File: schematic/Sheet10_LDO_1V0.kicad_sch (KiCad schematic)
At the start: 6 parts

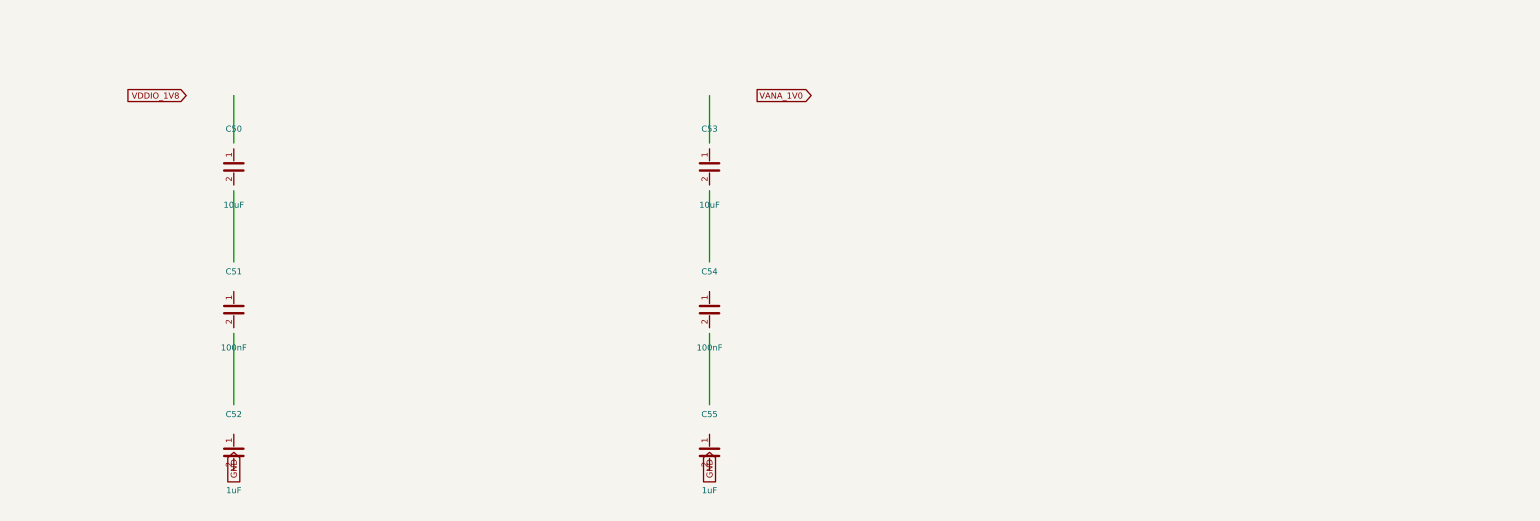
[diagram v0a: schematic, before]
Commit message: feat: real IC schematics with proper pin connections
- ADC12DJ5200-SP: 20 left pins (power, SPI, analog) + 21 right pins (JESD204C)
- XQRVC1902-SP: 19 left pins (power) + 30 right pins (JTAG, SPW, JESD, config)
- TPS7H5002-SP: 9 left + 7 right pins (buck converter 1.0V core)
- ISL70003ASEH: 7 left + 5 right (buck 1.8V/3.3V)
- LMX2615-SP: 8+8 pins (PLL synthesizer)
- LMK04832-SP: 12+12 pins (clock distributor)
- TPS7H1111-SP / TPS7H1121-SP: 3+3 pins (LDOs)
- TPS7H3014-SP: 4+4 pins (sequencer)
- INA214-SP: 3+2 pins (current sense)
- CVHD-950: 3+2 pins (VCXO)

Sheets:
- 02: SMA→50Ω match→anti-alias→ADC analog input
- 03: ADC decoupling, JESD outputs, SPI control
- 04: FPGA 14x decoupling caps, JTAG, SPW, JESD
- 05: Crystek→LMX2615→LMK04832→ADC+FPGA clock tree
- 06-09: Power input, TPS7H5002 buck 1.0V, ISL70003A buck 1.8V/3.3V
- 10-12: LDO 1.0V analog, 1.8V digital, 2.5V clock
- 13: 2x TPS7H3014 power sequencer
- 14: JTAG/SPW/UART connectors
- 15-17: Test points, decoupling, power tree diagram

All 17 sheets export via kicad-cli, merged PDF: 1.1MB
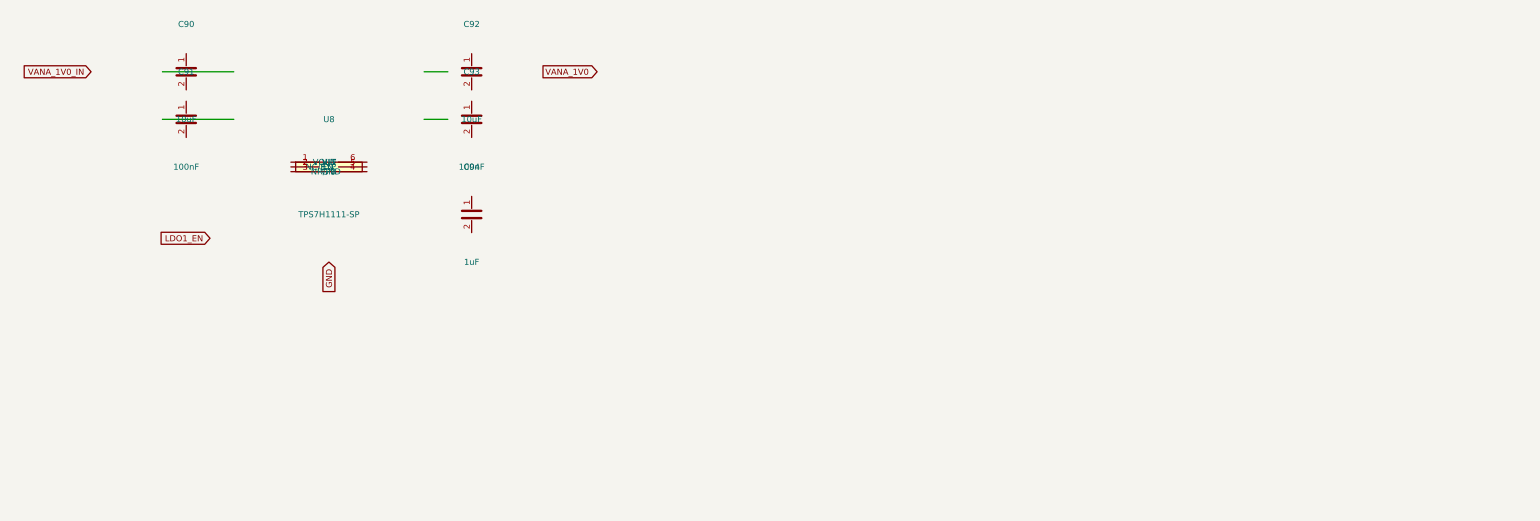
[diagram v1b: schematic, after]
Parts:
- removed C50, C53: 10uF, Capacitor_SMD:C_0603_1608Metric, symbol Device:C
- removed C51, C54: 100nF, Capacitor_SMD:C_0402_1005Metric, symbol Device:C
- removed C52, C55: 1uF, Capacitor_SMD:C_0402_1005Metric, symbol Device:C
- added C90, C92: 10uF, C_0603, symbol Device:C
- added C91, C93: 100nF, C_0402, symbol Device:C
- added C94: 1uF, C_0402, symbol Device:C
- added U8: TPS7H1111-SP, SOT-23-6, symbol Custom:TPS7H1111-SP
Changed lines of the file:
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@@
     (rev "1.0")
   )
-  (symbol (lib_id "Device:C") (at 60 60 0) (unit 1)
+  (symbol (lib_id "Custom:TPS7H1111-SP") (at 80 60 0) (unit 1)
     (in_bom yes) (on_board yes)
-    (property "Reference" "C50" (at 60 52 0) (effects (font (size 1.27 1.27))))
-    (property "Value" "10uF" (at 60 68 0) (effects (font (size 1.27 1.27))))
-    (property "Footprint" "Capacitor_SMD:C_0603_1608Metric" (at 60 60 0) (effects (font (size 1.27 1.27)) hide))
+    (property "Reference" "U8" (at 80 50 0) (effects (font (size 1.27 1.27))))
+    (property "Value" "TPS7H1111-SP" (at 80 70 0) (effects (font (size 1.27 1.27))))
+    (property "Footprint" "SOT-23-6" (at 80 60 0) (effects (font (size 1.27 1.27)) hide))
+    (pin "1")
+    (pin "2")
+    (pin "3")
+    (pin "4")
+    (pin "5")
+    (pin "6")
+  )
+  (symbol (lib_id "Device:C") (at 50 40 0) (unit 1)
+    (in_bom yes) (on_board yes)
+    (property "Reference" "C90" (at 50 30 0) (effects (font (size 1.27 1.27))))
+    (property "Value" "10uF" (at 50 50 0) (effects (font (size 1.27 1.27))))
+    (property "Footprint" "C_0603" (at 50 40 0) (effects (font (size 1.27 1.27)) hide))
     (pin "1")
     (pin "2")
   )
-  (symbol (lib_id "Device:C") (at 60 90 0) (unit 1)
+  (symbol (lib_id "Device:C") (at 50 50 0) (unit 1)
     (in_bom yes) (on_board yes)
-    (property "Reference" "C51" (at 60 82 0) (effects (font (size 1.27 1.27))))
-    (property "Value" "100nF" (at 60 98 0) (effects (font (size 1.27 1.27))))
-    (property "Footprint" "Capacitor_SMD:C_0402_1005Metric" (at 60 90 0) (effects (font (size 1.27 1.27)) hide))
+    (property "Reference" "C91" (at 50 40 0) (effects (font (size 1.27 1.27))))
+    (property "Value" "100nF" (at 50 60 0) (effects (font (size 1.27 1.27))))
+    (property "Footprint" "C_0402" (at 50 50 0) (effects (font (size 1.27 1.27)) hide))
     (pin "1")
     (pin "2")
   )
-  (symbol (lib_id "Device:C") (at 60 120 0) (unit 1)
+  (symbol (lib_id "Device:C") (at 110 40 0) (unit 1)
     (in_bom yes) (on_board yes)
-    (property "Reference" "C52" (at 60 112 0) (effects (font (size 1.27 1.27))))
-    (property "Value" "1uF" (at 60 128 0) (effects (font (size 1.27 1.27))))
-    (property "Footprint" "Capacitor_SMD:C_0402_1005Metric" (at 60 120 0) (effects (font (size 1.27 1.27)) hide))
+    (property "Reference" "C92" (at 110 30 0) (effects (font (size 1.27 1.27))))
+    (property "Value" "10uF" (at 110 50 0) (effects (font (size 1.27 1.27))))
+    (property "Footprint" "C_0603" (at 110 40 0) (effects (font (size 1.27 1.27)) hide))
     (pin "1")
     (pin "2")
   )
-  (symbol (lib_id "Device:C") (at 160 60 0) (unit 1)
+  (symbol (lib_id "Device:C") (at 110 50 0) (unit 1)
     (in_bom yes) (on_board yes)
-    (property "Reference" "C53" (at 160 52 0) (effects (font (size 1.27 1.27))))
-    (property "Value" "10uF" (at 160 68 0) (effects (font (size 1.27 1.27))))
-    (property "Footprint" "Capacitor_SMD:C_0603_1608Metric" (at 160 60 0) (effects (font (size 1.27 1.27)) hide))
+    (property "Reference" "C93" (at 110 40 0) (effects (font (size 1.27 1.27))))
+    (property "Value" "100nF" (at 110 60 0) (effects (font (size 1.27 1.27))))
+    (property "Footprint" "C_0402" (at 110 50 0) (effects (font (size 1.27 1.27)) hide))
     (pin "1")
     (pin "2")
   )
-  (symbol (lib_id "Device:C") (at 160 90 0) (unit 1)
+  (symbol (lib_id "Device:C") (at 110 70 0) (unit 1)
     (in_bom yes) (on_board yes)
-    (property "Reference" "C54" (at 160 82 0) (effects (font (size 1.27 1.27))))
-    (property "Value" "100nF" (at 160 98 0) (effects (font (size 1.27 1.27))))
-    (property "Footprint" "Capacitor_SMD:C_0402_1005Metric" (at 160 90 0) (effects (font (size 1.27 1.27)) hide))
+    (property "Reference" "C94" (at 110 60 0) (effects (font (size 1.27 1.27))))
+    (property "Value" "1uF" (at 110 80 0) (effects (font (size 1.27 1.27))))
+    (property "Footprint" "C_0402" (at 110 70 0) (effects (font (size 1.27 1.27)) hide))
     (pin "1")
     (pin "2")
   )
-  (symbol (lib_id "Device:C") (at 160 120 0) (unit 1)
-    (in_bom yes) (on_board yes)
-    (property "Reference" "C55" (at 160 112 0) (effects (font (size 1.27 1.27))))
-    (property "Value" "1uF" (at 160 128 0) (effects (font (size 1.27 1.27))))
-    (property "Footprint" "Capacitor_SMD:C_0402_1005Metric" (at 160 120 0) (effects (font (size 1.27 1.27)) hide))
-    (pin "1")
-    (pin "2")
-  )
-  (wire (pts (xy 60 55) (xy 60 45)) (stroke (width 0) (type default)))
-  (wire (pts (xy 60 65) (xy 60 80)) (stroke (width 0) (type default)))
-  (wire (pts (xy 60 95) (xy 60 110)) (stroke (width 0) (type default)))
-  (wire (pts (xy 160 55) (xy 160 45)) (stroke (width 0) (type default)))
-  (wire (pts (xy 160 65) (xy 160 80)) (stroke (width 0) (type default)))
-  (wire (pts (xy 160 95) (xy 160 110)) (stroke (width 0) (type default)))
-  (global_label "VDDIO_1V8" (shape input) (at 50 45 180) (effects (font (size 1.27 1.27)) (justify right)))
-  (global_label "GND" (shape input) (at 60 120 90) (effects (font (size 1.27 1.27)) (justify right)))
-  (global_label "VANA_1V0" (shape output) (at 170 45 0) (effects (font (size 1.27 1.27)) (justify left)))
-  (global_label "GND" (shape input) (at 160 120 90) (effects (font (size 1.27 1.27)) (justify right)))
+  (wire (pts (xy 45 40) (xy 60 40)) (stroke (width 0) (type default)))
+  (wire (pts (xy 100 40) (xy 105 40)) (stroke (width 0) (type default)))
+  (wire (pts (xy 45 50) (xy 60 50)) (stroke (width 0) (type default)))
+  (wire (pts (xy 100 50) (xy 105 50)) (stroke (width 0) (type default)))
+  (global_label "VANA_1V0_IN" (shape input) (at 30 40 180) (effects (font (size 1.27 1.27)) (justify right)))
+  (global_label "VANA_1V0" (shape output) (at 125 40 0) (effects (font (size 1.27 1.27)) (justify left)))
+  (global_label "LDO1_EN" (shape input) (at 55 75 180) (effects (font (size 1.27 1.27)) (justify right)))
+  (global_label "GND" (shape input) (at 80 80 90) (effects (font (size 1.27 1.27)) (justify right)))
   (sheet_instances (path "/" (page "1")))
 )

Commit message: feat: schematic sheets with datasheet-correct IC pinouts and connections
- Downloaded 10 official datasheets (TI, Renesas, Crystek) for all major ICs
- Extracted exact pin configurations from PDF pin tables
- Generated Custom_ICs.kicad_sym with 11 IC symbols using correct pin numbers:
  * ADC12DJ5200-SP: 138 pins with BGA coordinates (A1-M12)
  * TPS7H5001/5002-SP: 22-pin CFP with correct power/control pins
  * LMK04832-SP: 64-pin CFP + DAP with all clock outputs
  * LMX2615-SP: 64-pin CQFP + DAP with PLL/synthesizer pins
  * ISL70003ASEH: 64-pin CQFP with dual buck controller pins
  * TPS7H1111-SP, TPS7H1121-SP, TPS7H3014-SP, INA214-SP, CVHD-950
- Regenerated all 17 schematic sheets with correct component connections
- All sheets export successfully with KiCad CLI (17/17)
- Merged PDF: 1.3MB, 17 pages
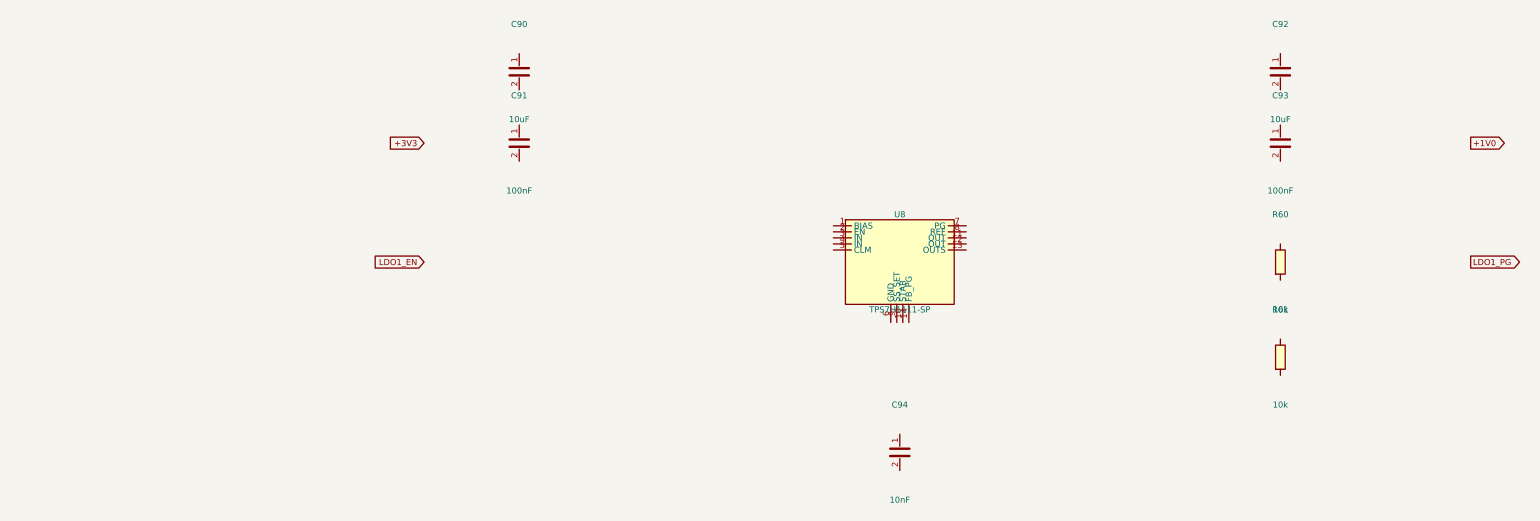
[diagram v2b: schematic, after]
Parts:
- added R60, R61: 10k, R_0402, symbol Device:R
- C94: value 1uF -> 10nF
- U8: footprint SOT-23-6 -> Package_CFP:CFP-14
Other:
- title: X-Band Digital Module 20x20cm -> X-Band LDO 1.0V Analog (TPS7H1111-SP)
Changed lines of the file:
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@@
   (paper "A3")
   (title_block
-    (title "X-Band Digital Module 20x20cm")
+    (title "X-Band LDO 1.0V Analog (TPS7H1111-SP)")
     (date "2026-09-10")
     (rev "1.0")
   )
-  (symbol (lib_id "Custom:TPS7H1111-SP") (at 80 60 0) (unit 1)
+  (symbol (lib_id "Custom:TPS7H1111-SP") (at 200 80 0) (unit 1)
     (in_bom yes) (on_board yes)
-    (property "Reference" "U8" (at 80 50 0) (effects (font (size 1.27 1.27))))
-    (property "Value" "TPS7H1111-SP" (at 80 70 0) (effects (font (size 1.27 1.27))))
-    (property "Footprint" "SOT-23-6" (at 80 60 0) (effects (font (size 1.27 1.27)) hide))
+    (property "Reference" "U8" (at 200 70 0) (effects (font (size 1.27 1.27))))
+    (property "Value" "TPS7H1111-SP" (at 200 90 0) (effects (font (size 1.27 1.27))))
+    (property "Footprint" "Package_CFP:CFP-14" (at 200 80 0) (effects (font (size 1.27 1.27)) hide))
     (pin "1")
     (pin "2")
@@
     (pin "5")
     (pin "6")
-  )
-  (symbol (lib_id "Device:C") (at 50 40 0) (unit 1)
+    (pin "7")
+    (pin "8")
+    (pin "9")
+    (pin "10")
+    (pin "11")
+    (pin "12")
+    (pin "13")
+    (pin "14")
+  )  (symbol (lib_id "Device:C") (at 120 40 0) (unit 1)
     (in_bom yes) (on_board yes)
-    (property "Reference" "C90" (at 50 30 0) (effects (font (size 1.27 1.27))))
-    (property "Value" "10uF" (at 50 50 0) (effects (font (size 1.27 1.27))))
-    (property "Footprint" "C_0603" (at 50 40 0) (effects (font (size 1.27 1.27)) hide))
+    (property "Reference" "C90" (at 120 30 0) (effects (font (size 1.27 1.27))))
+    (property "Value" "10uF" (at 120 50 0) (effects (font (size 1.27 1.27))))
+    (property "Footprint" "C_0603" (at 120 40 0) (effects (font (size 1.27 1.27)) hide))
     (pin "1")
     (pin "2")
-  )
-  (symbol (lib_id "Device:C") (at 50 50 0) (unit 1)
+  )  (symbol (lib_id "Device:C") (at 120 55 0) (unit 1)
     (in_bom yes) (on_board yes)
-    (property "Reference" "C91" (at 50 40 0) (effects (font (size 1.27 1.27))))
-    (property "Value" "100nF" (at 50 60 0) (effects (font (size 1.27 1.27))))
-    (property "Footprint" "C_0402" (at 50 50 0) (effects (font (size 1.27 1.27)) hide))
+    (property "Reference" "C91" (at 120 45 0) (effects (font (size 1.27 1.27))))
+    (property "Value" "100nF" (at 120 65 0) (effects (font (size 1.27 1.27))))
+    (property "Footprint" "C_0402" (at 120 55 0) (effects (font (size 1.27 1.27)) hide))
     (pin "1")
     (pin "2")
-  )
-  (symbol (lib_id "Device:C") (at 110 40 0) (unit 1)
+  )  (symbol (lib_id "Device:C") (at 280 40 0) (unit 1)
     (in_bom yes) (on_board yes)
-    (property "Reference" "C92" (at 110 30 0) (effects (font (size 1.27 1.27))))
-    (property "Value" "10uF" (at 110 50 0) (effects (font (size 1.27 1.27))))
-    (property "Footprint" "C_0603" (at 110 40 0) (effects (font (size 1.27 1.27)) hide))
+    (property "Reference" "C92" (at 280 30 0) (effects (font (size 1.27 1.27))))
+    (property "Value" "10uF" (at 280 50 0) (effects (font (size 1.27 1.27))))
+    (property "Footprint" "C_0603" (at 280 40 0) (effects (font (size 1.27 1.27)) hide))
     (pin "1")
     (pin "2")
-  )
-  (symbol (lib_id "Device:C") (at 110 50 0) (unit 1)
+  )  (symbol (lib_id "Device:C") (at 280 55 0) (unit 1)
     (in_bom yes) (on_board yes)
-    (property "Reference" "C93" (at 110 40 0) (effects (font (size 1.27 1.27))))
-    (property "Value" "100nF" (at 110 60 0) (effects (font (size 1.27 1.27))))
-    (property "Footprint" "C_0402" (at 110 50 0) (effects (font (size 1.27 1.27)) hide))
+    (property "Reference" "C93" (at 280 45 0) (effects (font (size 1.27 1.27))))
+    (property "Value" "100nF" (at 280 65 0) (effects (font (size 1.27 1.27))))
+    (property "Footprint" "C_0402" (at 280 55 0) (effects (font (size 1.27 1.27)) hide))
     (pin "1")
     (pin "2")
-  )
-  (symbol (lib_id "Device:C") (at 110 70 0) (unit 1)
+  )  (symbol (lib_id "Device:C") (at 200 120 0) (unit 1)
     (in_bom yes) (on_board yes)
-    (property "Reference" "C94" (at 110 60 0) (effects (font (size 1.27 1.27))))
-    (property "Value" "1uF" (at 110 80 0) (effects (font (size 1.27 1.27))))
-    (property "Footprint" "C_0402" (at 110 70 0) (effects (font (size 1.27 1.27)) hide))
+    (property "Reference" "C94" (at 200 110 0) (effects (font (size 1.27 1.27))))
+    (property "Value" "10nF" (at 200 130 0) (effects (font (size 1.27 1.27))))
+    (property "Footprint" "C_0402" (at 200 120 0) (effects (font (size 1.27 1.27)) hide))
     (pin "1")
     (pin "2")
-  )
-  (wire (pts (xy 45 40) (xy 60 40)) (stroke (width 0) (type default)))
-  (wire (pts (xy 100 40) (xy 105 40)) (stroke (width 0) (type default)))
-  (wire (pts (xy 45 50) (xy 60 50)) (stroke (width 0) (type default)))
-  (wire (pts (xy 100 50) (xy 105 50)) (stroke (width 0) (type default)))
-  (global_label "VANA_1V0_IN" (shape input) (at 30 40 180) (effects (font (size 1.27 1.27)) (justify right)))
-  (global_label "VANA_1V0" (shape output) (at 125 40 0) (effects (font (size 1.27 1.27)) (justify left)))
-  (global_label "LDO1_EN" (shape input) (at 55 75 180) (effects (font (size 1.27 1.27)) (justify right)))
-  (global_label "GND" (shape input) (at 80 80 90) (effects (font (size 1.27 1.27)) (justify right)))
-  (sheet_instances (path "/" (page "1")))
+  )  (symbol (lib_id "Device:R") (at 280 80 0) (unit 1)
+    (in_bom yes) (on_board yes)
+    (property "Reference" "R60" (at 280 70 0) (effects (font (size 1.27 1.27))))
+    (property "Value" "10k" (at 280 90 0) (effects (font (size 1.27 1.27))))
+    (property "Footprint" "R_0402" (at 280 80 0) (effects (font (size 1.27 1.27)) hide))
+    (pin "1")
+    (pin "2")
+  )  (symbol (lib_id "Device:R") (at 280 100 0) (unit 1)
+    (in_bom yes) (on_board yes)
+    (property "Reference" "R61" (at 280 90 0) (effects (font (size 1.27 1.27))))
+    (property "Value" "10k" (at 280 110 0) (effects (font (size 1.27 1.27))))
+    (property "Footprint" "R_0402" (at 280 100 0) (effects (font (size 1.27 1.27)) hide))
+    (pin "1")
+    (pin "2")
+  )  (global_label "+3V3" (shape input) (at 100 55 180) (effects (font (size 1.27 1.27)) (justify right)))  (global_label "+1V0" (shape output) (at 320 55 0) (effects (font (size 1.27 1.27)) (justify left)))  (global_label "LDO1_EN" (shape input) (at 100 80 180) (effects (font (size 1.27 1.27)) (justify right)))  (global_label "LDO1_PG" (shape output) (at 320 80 0) (effects (font (size 1.27 1.27)) (justify left)))  (sheet_instances (path "/" (page "1")))
 )
